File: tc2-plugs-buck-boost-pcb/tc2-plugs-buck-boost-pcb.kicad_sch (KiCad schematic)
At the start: 61 parts, among them J201 JCON_M16_04Pin, J202 JCON_M16_2+4Pin, J203 Conn_02x06_Odd_Even, Q201 Q_PMOS_GSD, Q202 Q_PMOS_GSD, Q203 AO3400A, U201 TPS63070RNMR, U202 TPS63071

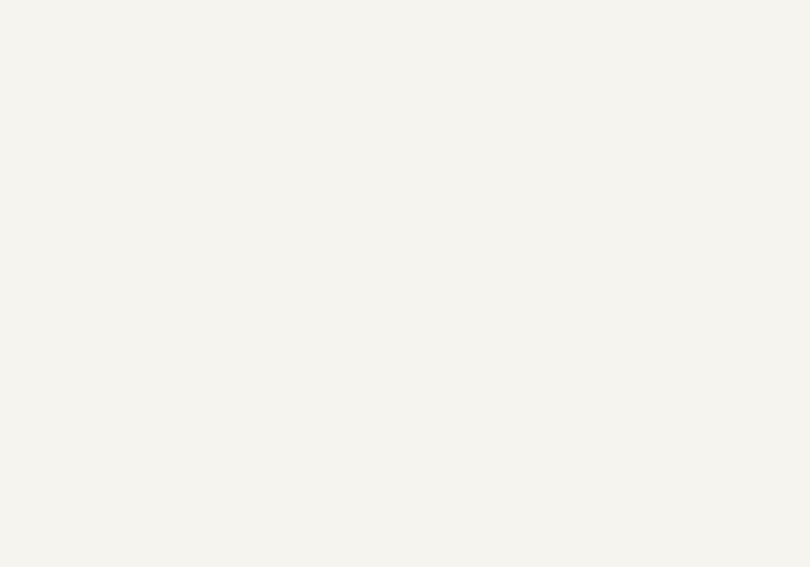
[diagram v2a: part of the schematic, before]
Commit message: Add JLPCPCB 2D barcode to PCBs
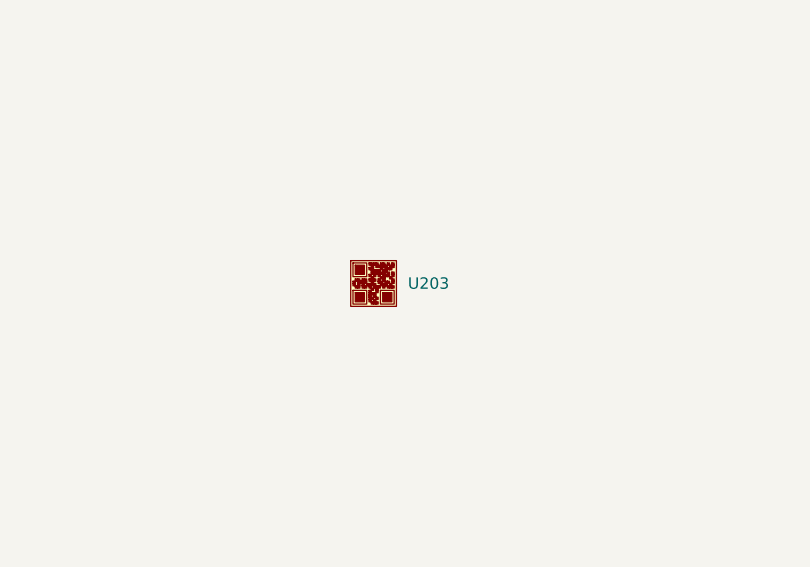
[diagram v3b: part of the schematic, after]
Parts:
- added U203: (no value), cacophony-library:JLCPCB_QR_8mm, symbol cacophony-library:JLCPCB_QR_CODE
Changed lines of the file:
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@@
+	)
+	(symbol
+		(lib_id "cacophony-library:JLCPCB_QR_CODE")
+		(at 107.95 110.49 0)
+		(unit 1)
+		(body_style 1)
+		(exclude_from_sim yes)
+		(in_bom no)
+		(on_board yes)
+		(in_pos_files no)
+		(dnp no)
+		(fields_autoplaced yes)
+		(property "Reference" "U203"
+			(at 111.76 110.4899 0)
+			(show_name no)
+			(do_not_autoplace no)
+			(effects
+				(font
+					(size 1.27 1.27)
+				)
+				(justify left)
+			)
+		)
+		(property "Value" ""
+			(at 107.95 110.49 0)
+			(show_name no)
+			(do_not_autoplace no)
+			(effects
+				(font
+					(size 1.27 1.27)
+				)
+			)
+		)
+		(property "Footprint" "cacophony-library:JLCPCB_QR_8mm"
+			(at 107.95 110.49 0)
+			(hide yes)
+			(show_name no)
+			(do_not_autoplace no)
+			(effects
+				(font
+					(size 1.27 1.27)
+				)
+			)
+		)
+		(property "Datasheet" ""
+			(at 107.95 110.49 0)
+			(hide yes)
+			(show_name no)
+			(do_not_autoplace no)
+			(effects
+				(font
+					(size 1.27 1.27)
+				)
+			)
+		)
+		(property "Description" ""
+			(at 107.95 110.49 0)
+			(hide yes)
+			(show_name no)
+			(do_not_autoplace no)
+			(effects
+				(font
+					(size 1.27 1.27)
+				)
+			)
+		)
+		(instances
+			(project "tc2-plugs-buck-boost-pcb"
+				(path "/f421ea14-42dc-4485-8e12-78680a358584"
+					(reference "U203")
+					(unit 1)
+				)
+			)
+		)
 	)
 	(symbol

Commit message: Set inductor values
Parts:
- L201, L202: value INDUCTOR -> 1.5uH
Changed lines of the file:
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@@
 			)
 		)
-		(property "Value" "INDUCTOR"
+		(property "Value" "1.5uH"
 			(at 273.05 166.37 0)
 			(show_name no)
@@
 			)
 		)
-		(property "Value" "INDUCTOR"
+		(property "Value" "1.5uH"
 			(at 273.05 87.63 0)
 			(show_name no)

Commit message: Update 5V DC-DC buck-boost
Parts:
- R212: value 680k -> 150k; LCSC Part (none) -> C723770; now fitted; now in the parts list
- R214: value 130k -> 820k; LCSC Part (none) -> C4042952; now fitted; now in the parts list
- U202: value TPS63071 -> TPS63070; symbol cacophony-library:TPS63071 -> cacophony-library:TPS63070RNMR; LCSC Part C2876599 -> C109322
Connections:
- net 5V_PHY: now also R214.1; no longer R212.1, U202.5 (FB)
- net GND: now also R212.2; no longer R214.2
- new net: R212.1, R214.2, U202.5 (FB)
- no-connect marks 4 -> 2
